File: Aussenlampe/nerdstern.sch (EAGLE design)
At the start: 10 parts, among them K1 G6RS

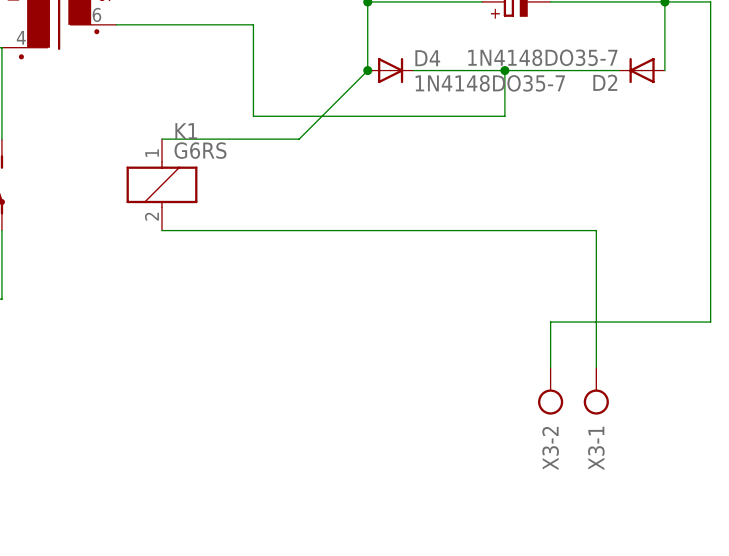
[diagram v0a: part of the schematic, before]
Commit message: add optocopler, wirin still questionable
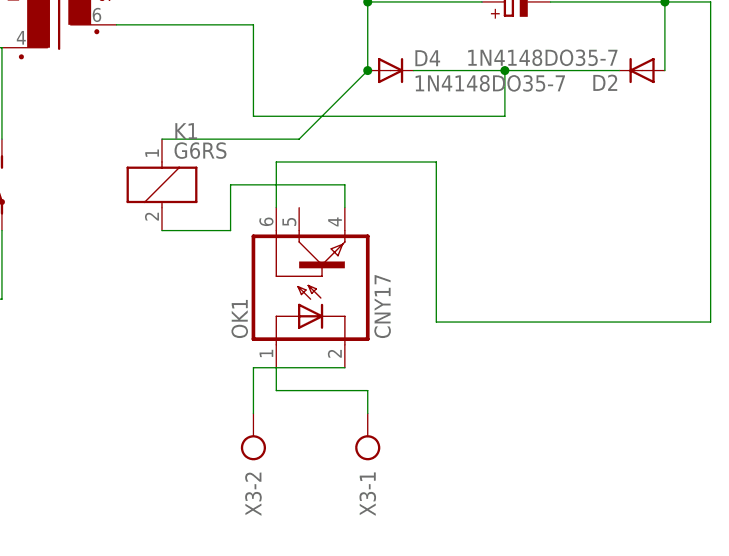
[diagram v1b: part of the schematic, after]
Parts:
- added OK1: CNY17, optocoupler:CNY17
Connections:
- removed net GND: K11.2, X3-1.KL
- new net N$10: OK1.A, X3-1.KL
- new net N$11: OK1.C, X3-2.KL
- new net N$12: K11.2, OK1.EMI
- net N$6: now also OK1.BAS; no longer X3-2.KL
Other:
- moved on the sheet: X3-1, X3-2
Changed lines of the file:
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@@
 <part name="X2" library="con-ptr500" deviceset="AK500/3" device=""/>
 <part name="X3" library="con-ptr500" deviceset="AK500/2" device=""/>
+<part name="OK1" library="optocoupler" deviceset="CNY17" device=""/>
 </parts>
 <sheets>
@@
 <instance part="X2" gate="-2" x="5.08" y="33.02"/>
 <instance part="X2" gate="-3" x="5.08" y="27.94"/>
-<instance part="X3" gate="-1" x="88.9" y="20.32" rot="R90"/>
-<instance part="X3" gate="-2" x="83.82" y="20.32" rot="R90"/>
+<instance part="X3" gate="-1" x="63.5" y="15.24" rot="R90"/>
+<instance part="X3" gate="-2" x="50.8" y="15.24" rot="R90"/>
+<instance part="OK1" gate="G$1" x="55.88" y="35.56" rot="R90"/>
 </instances>
 <busses>
@@
 <wire x1="101.6" y1="66.04" x2="101.6" y2="30.48" width="0.1524" layer="91"/>
 <junction x="96.52" y="66.04"/>
-<pinref part="X3" gate="-2" pin="KL"/>
-<wire x1="83.82" y1="25.4" x2="83.82" y2="30.48" width="0.1524" layer="91"/>
-<wire x1="83.82" y1="30.48" x2="101.6" y2="30.48" width="0.1524" layer="91"/>
+<wire x1="101.6" y1="30.48" x2="71.12" y2="30.48" width="0.1524" layer="91"/>
+<wire x1="71.12" y1="30.48" x2="71.12" y2="48.26" width="0.1524" layer="91"/>
+<pinref part="OK1" gate="G$1" pin="BAS"/>
+<wire x1="71.12" y1="48.26" x2="53.34" y2="48.26" width="0.1524" layer="91"/>
+<wire x1="53.34" y1="48.26" x2="53.34" y2="43.18" width="0.1524" layer="91"/>
 </segment>
 </net>
@@
 </segment>
 </net>
-<net name="GND" class="0">
-<segment>
-<pinref part="K1" gate="1" pin="2"/>
-<wire x1="40.64" y1="40.64" x2="88.9" y2="40.64" width="0.1524" layer="91"/>
-<pinref part="X3" gate="-1" pin="KL"/>
-<wire x1="88.9" y1="40.64" x2="88.9" y2="25.4" width="0.1524" layer="91"/>
-</segment>
-</net>
 <net name="N$8" class="0">
 <segment>
@@
 </segment>
 </net>
+<net name="N$10" class="0">
+<segment>
+<pinref part="OK1" gate="G$1" pin="A"/>
+<wire x1="53.34" y1="25.4" x2="53.34" y2="22.86" width="0.1524" layer="91"/>
+<pinref part="X3" gate="-1" pin="KL"/>
+<wire x1="53.34" y1="22.86" x2="63.5" y2="22.86" width="0.1524" layer="91"/>
+<wire x1="63.5" y1="22.86" x2="63.5" y2="20.32" width="0.1524" layer="91"/>
+</segment>
+</net>
+<net name="N$11" class="0">
+<segment>
+<pinref part="OK1" gate="G$1" pin="C"/>
+<pinref part="X3" gate="-2" pin="KL"/>
+<wire x1="60.96" y1="25.4" x2="50.8" y2="25.4" width="0.1524" layer="91"/>
+<wire x1="50.8" y1="25.4" x2="50.8" y2="20.32" width="0.1524" layer="91"/>
+</segment>
+</net>
+<net name="N$12" class="0">
+<segment>
+<pinref part="K1" gate="1" pin="2"/>
+<wire x1="40.64" y1="40.64" x2="48.26" y2="40.64" width="0.1524" layer="91"/>
+<wire x1="48.26" y1="40.64" x2="48.26" y2="45.72" width="0.1524" layer="91"/>
+<pinref part="OK1" gate="G$1" pin="EMI"/>
+<wire x1="48.26" y1="45.72" x2="60.96" y2="45.72" width="0.1524" layer="91"/>
+<wire x1="60.96" y1="45.72" x2="60.96" y2="43.18" width="0.1524" layer="91"/>
+</segment>
+</net>

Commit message: routing and some repositioning of parts
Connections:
- net N$3: now also X2-3.KL; no longer X2-1.KL
- net N$8: now also X2-1.KL; no longer X2-3.KL
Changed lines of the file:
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@@
 <wire x1="22.86" y1="50.8" x2="22.86" y2="60.96" width="0.1524" layer="91"/>
 <junction x="10.16" y="78.74"/>
+<junction x="22.86" y="60.96"/>
 </segment>
 </net>
@@
 <wire x1="22.86" y1="83.82" x2="20.32" y2="83.82" width="0.1524" layer="91"/>
 <wire x1="20.32" y1="83.82" x2="10.16" y2="83.82" width="0.1524" layer="91"/>
-<wire x1="10.16" y1="38.1" x2="20.32" y2="38.1" width="0.1524" layer="91"/>
-<wire x1="20.32" y1="38.1" x2="20.32" y2="83.82" width="0.1524" layer="91"/>
+<wire x1="20.32" y1="27.94" x2="20.32" y2="83.82" width="0.1524" layer="91"/>
 <junction x="20.32" y="83.82"/>
-<pinref part="X2" gate="-1" pin="KL"/>
 <junction x="10.16" y="83.82"/>
-<junction x="10.16" y="38.1"/>
+<pinref part="X2" gate="-3" pin="KL"/>
+<wire x1="20.32" y1="27.94" x2="10.16" y2="27.94" width="0.1524" layer="91"/>
 </segment>
 </net>
@@
 <pinref part="X1" gate="-3" pin="KL"/>
 <wire x1="10.16" y1="73.66" x2="15.24" y2="73.66" width="0.1524" layer="91"/>
-<wire x1="15.24" y1="73.66" x2="15.24" y2="27.94" width="0.1524" layer="91"/>
-<pinref part="X2" gate="-3" pin="KL"/>
-<wire x1="15.24" y1="27.94" x2="10.16" y2="27.94" width="0.1524" layer="91"/>
+<wire x1="15.24" y1="73.66" x2="15.24" y2="38.1" width="0.1524" layer="91"/>
 <junction x="10.16" y="73.66"/>
+<pinref part="X2" gate="-1" pin="KL"/>
+<wire x1="10.16" y1="38.1" x2="15.24" y2="38.1" width="0.1524" layer="91"/>
 </segment>
 </net>

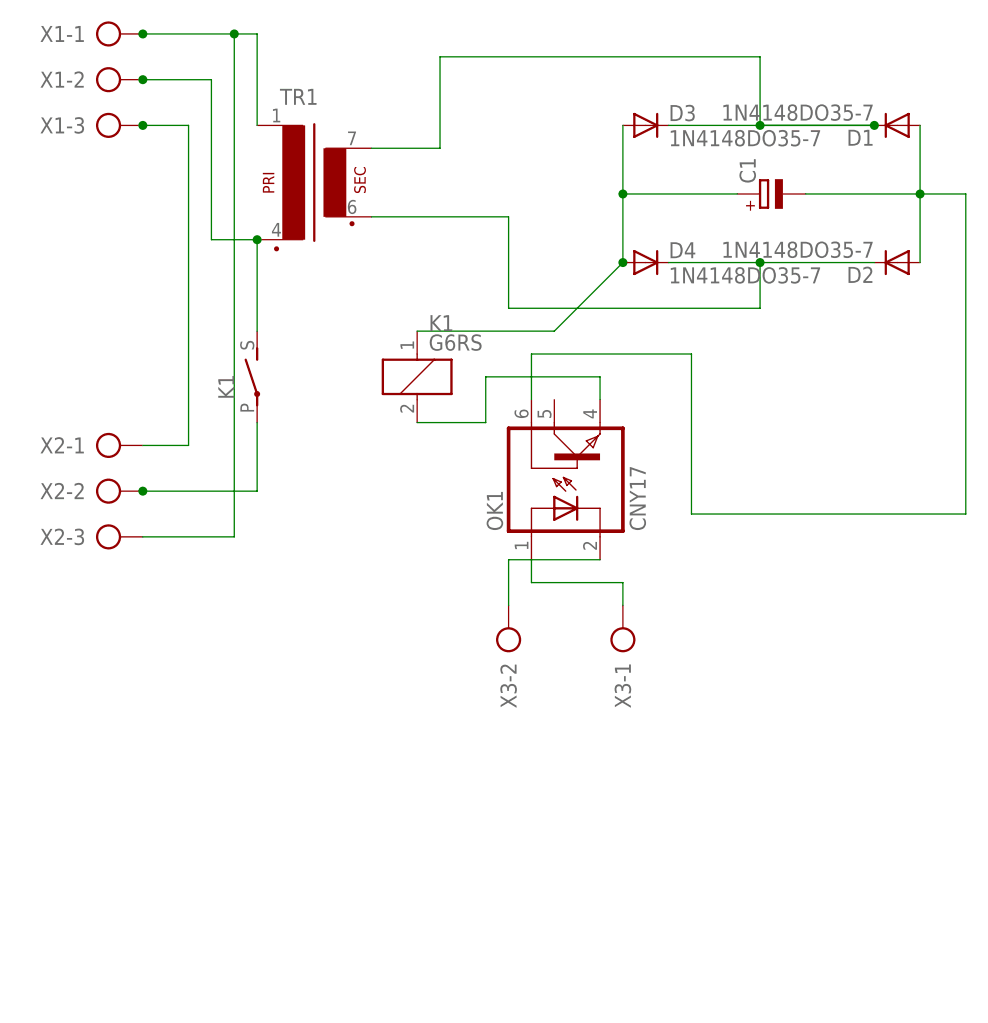
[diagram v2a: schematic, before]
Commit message: schaltplan korrigiert
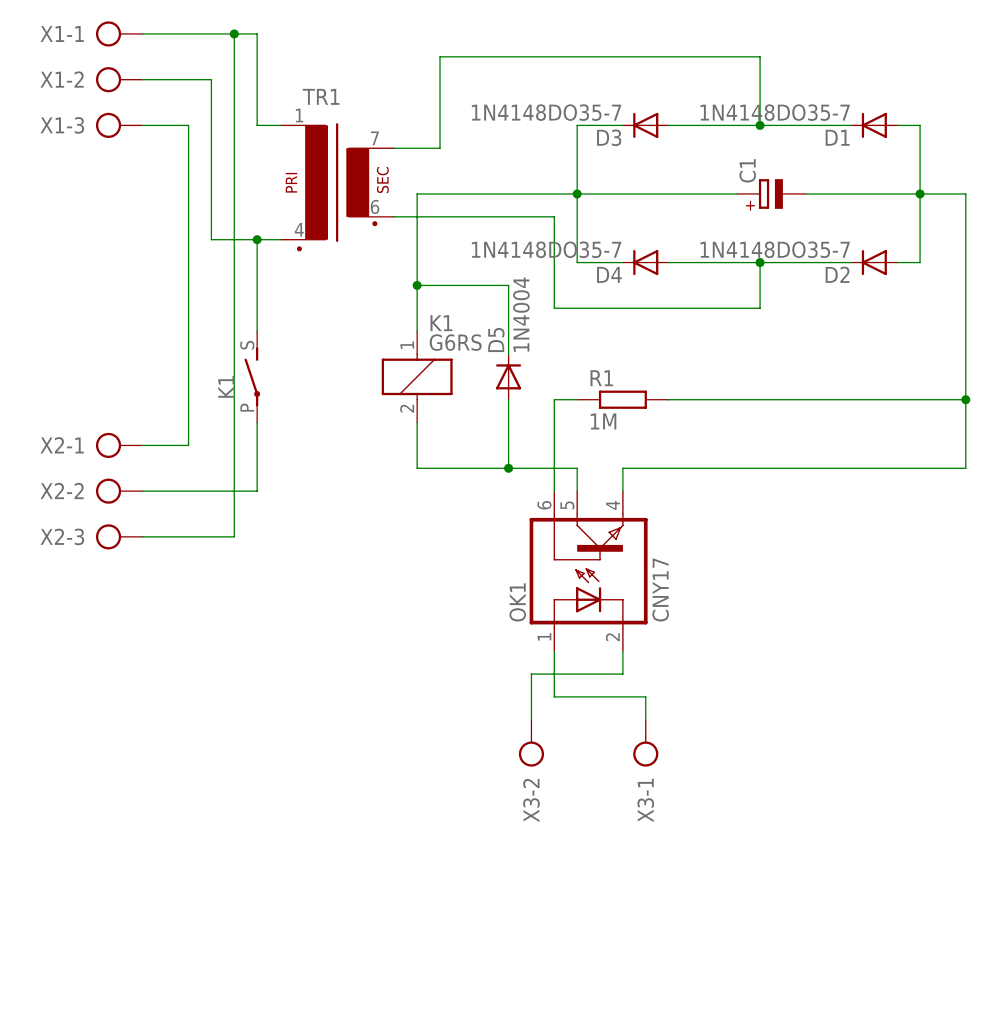
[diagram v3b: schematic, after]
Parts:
- added D5: 1N4004, diode:1N4004
- added R1: 1M, rcl:R-EU_0204/5
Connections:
- removed net N$6: C1.-, D1.A, D2.A, OK1.BAS
- new net GND: C1.-, D1.A, D2.A, OK1.EMI, R1.2
- new net N$14: OK1.BAS, R1.1
- net N$12: now also D5.A, OK1.COL; no longer OK1.EMI
- net N$4: now also D3.A; no longer D3.C
- net N$5: now also D3.C, D4.C, D5.C; no longer D3.A, D4.A
- net N$7: now also D4.A; no longer D4.C
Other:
- moved on the sheet: D1, D2, D3, D4, OK1, TR1, X3-1, X3-2

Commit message: routing
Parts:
- added R2: 1K, rcl:R-EU_0204/5
- C1: value (none) -> 33u
- D1, D2, D3, D4: value 1N4148DO35-7 -> 1N4148
- D5: value 1N4004 -> 1N4001; device diode:1N4004 -> diode:1N4148DO35-7
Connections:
- net N$8 renamed GND2
- new net N$15: R2.2, X3-1.KL
- net N$10: now also R2.1; no longer X3-1.KL
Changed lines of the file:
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@@
 <parts>
 <part name="TR1" library="trafo" deviceset="EE20-1" device=""/>
-<part name="D1" library="diode" deviceset="1N4148" device="DO35-7"/>
-<part name="D2" library="diode" deviceset="1N4148" device="DO35-7"/>
-<part name="D3" library="diode" deviceset="1N4148" device="DO35-7"/>
-<part name="D4" library="diode" deviceset="1N4148" device="DO35-7"/>
-<part name="C1" library="rcl" deviceset="CPOL-EU" device="E2-5"/>
+<part name="D1" library="diode" deviceset="1N4148" device="DO35-7" value="1N4148"/>
+<part name="D2" library="diode" deviceset="1N4148" device="DO35-7" value="1N4148"/>
+<part name="D3" library="diode" deviceset="1N4148" device="DO35-7" value="1N4148"/>
+<part name="D4" library="diode" deviceset="1N4148" device="DO35-7" value="1N4148"/>
+<part name="C1" library="rcl" deviceset="CPOL-EU" device="E2-5" value="33u"/>
 <part name="K1" library="relay" deviceset="G6RS" device=""/>
 <part name="X1" library="con-ptr500" deviceset="AK500/3" device=""/>
@@
 <part name="OK1" library="optocoupler" deviceset="CNY17" device=""/>
 <part name="R1" library="rcl" deviceset="R-EU_" device="0204/5" value="1M"/>
-<part name="D5" library="diode" deviceset="1N4004" device=""/>
+<part name="R2" library="rcl" deviceset="R-EU_" device="0204/5" value="1K"/>
+<part name="D5" library="diode" deviceset="1N4148" device="DO35-7" value="1N4001"/>
 </parts>
 <sheets>
@@
 <instance part="OK1" gate="G$1" x="58.42" y="25.4" rot="R90"/>
 <instance part="R1" gate="G$1" x="63.5" y="43.18"/>
-<instance part="D5" gate="1" x="50.8" y="45.72" rot="R90"/>
+<instance part="R2" gate="G$1" x="60.96" y="10.16"/>
+<instance part="D5" gate="G$1" x="50.8" y="45.72" rot="R90"/>
 </instances>
 <busses>
@@
 <wire x1="40.64" y1="66.04" x2="58.42" y2="66.04" width="0.1524" layer="91"/>
 <junction x="58.42" y="66.04"/>
-<pinref part="D5" gate="1" pin="C"/>
 <wire x1="50.8" y1="48.26" x2="50.8" y2="55.88" width="0.1524" layer="91"/>
 <wire x1="50.8" y1="55.88" x2="40.64" y2="55.88" width="0.1524" layer="91"/>
 <junction x="40.64" y="55.88"/>
+<pinref part="D5" gate="G$1" pin="C"/>
 </segment>
 </net>
@@
 </segment>
 </net>
-<net name="N$8" class="0">
+<net name="GND2" class="0">
 <segment>
 <pinref part="X1" gate="-3" pin="KL"/>
@@
 <pinref part="OK1" gate="G$1" pin="A"/>
 <wire x1="55.88" y1="15.24" x2="55.88" y2="10.16" width="0.1524" layer="91"/>
-<pinref part="X3" gate="-1" pin="KL"/>
-<wire x1="55.88" y1="10.16" x2="66.04" y2="10.16" width="0.1524" layer="91"/>
-<wire x1="66.04" y1="10.16" x2="66.04" y2="7.62" width="0.1524" layer="91"/>
+<pinref part="R2" gate="G$1" pin="1"/>
 </segment>
 </net>
 <net name="N$11" class="0">
 <segment>
+<pinref part="X3" gate="-2" pin="KL"/>
+<wire x1="53.34" y1="12.7" x2="53.34" y2="7.62" width="0.1524" layer="91"/>
 <pinref part="OK1" gate="G$1" pin="C"/>
-<pinref part="X3" gate="-2" pin="KL"/>
 <wire x1="63.5" y1="15.24" x2="63.5" y2="12.7" width="0.1524" layer="91"/>
-<wire x1="63.5" y1="12.7" x2="53.34" y2="12.7" width="0.1524" layer="91"/>
-<wire x1="53.34" y1="12.7" x2="53.34" y2="7.62" width="0.1524" layer="91"/>
+<wire x1="53.34" y1="12.7" x2="63.5" y2="12.7" width="0.1524" layer="91"/>
 </segment>
 </net>
@@
 <wire x1="50.8" y1="35.56" x2="58.42" y2="35.56" width="0.1524" layer="91"/>
 <wire x1="58.42" y1="35.56" x2="58.42" y2="33.02" width="0.1524" layer="91"/>
-<pinref part="D5" gate="1" pin="A"/>
 <wire x1="50.8" y1="43.18" x2="50.8" y2="35.56" width="0.1524" layer="91"/>
 <junction x="50.8" y="35.56"/>
-</segment>
-</net>
+<pinref part="D5" gate="G$1" pin="A"/>
+</segment>
+</net>
+<net name="N$15" class="0">
+<segment>
+<pinref part="X3" gate="-1" pin="KL"/>
+<wire x1="66.04" y1="10.16" x2="66.04" y2="7.62" width="0.1524" layer="91"/>
+<pinref part="R2" gate="G$1" pin="2"/>
+</segment>
+</net>
